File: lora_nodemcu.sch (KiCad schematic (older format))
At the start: 17 parts, among them U1 RFM95, U2 LM1117-3.3, U3 WeMos_mini

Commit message: fixed non connect on schematic and moved decoupling caps closer
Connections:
- net labels added: RF95_3V3, wemos_5V
- wire segments 65 -> 75
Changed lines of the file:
@@
 	4450 3500 4450 3950
 Wire Wire Line
-	3940 3400 4500 3400
+	3940 3400 3990 3400
 Wire Wire Line
 	5700 3500 5800 3500
@@
 	5800 3500 5800 3650
 Wire Wire Line
-	3910 3100 4500 3100
+	3910 3100 3990 3100
 Wire Wire Line
 	5900 3300 5700 3300
@@
 Wire Wire Line
 	5700 2800 5700 2700
-Wire Wire Line
-	7700 2150 7700 2500
 Wire Wire Line
 	7700 2500 7850 2500
@@
 	7000 3550 7000 3100
 Wire Wire Line
-	8100 4550 8600 4550
+	8100 4550 8350 4550
 Wire Wire Line
-	7050 4550 7500 4550
+	7050 4550 7300 4550
 Wire Wire Line
-	7800 4850 7800 5150
+	7800 4850 7800 5000
 Wire Wire Line
 	7300 4700 7300 4550
@@
 Connection ~ 8350 4550
 Wire Wire Line
-	7300 5000 8350 5000
+	7300 5000 7800 5000
 Wire Wire Line
 	8350 5000 8350 4900
 Connection ~ 7800 5000
 Wire Wire Line
-	8100 4475 8100 4650
+	8100 4475 8100 4550
 Connection ~ 8100 4550
 Wire Wire Line
@@
 	7160 2900 7850 2900
 Wire Wire Line
-	7380 2600 7380 2170
-Wire Wire Line
-	7700 1840 7700 1940
+	7380 2600 7380 2330
 Wire Wire Line
 	7700 2330 7630 2330
-Connection ~ 7700 2330
 Wire Wire Line
 	7430 2330 7380 2330
@@
 L device:C_Small C5
 U 1 1 5A1F028E
-P 9060 2310
-F 0 "C5" V 8831 2310 50  0000 C CNN
-F 1 "C_decoupling" V 8922 2310 50  0000 C CNN
-F 2 "Capacitors_SMD:C_0805_HandSoldering" H 9060 2310 50  0001 C CNN
-F 3 "" H 9060 2310 50  0001 C CNN
-	1    9060 2310
+P 9110 2310
+F 0 "C5" V 8881 2310 50  0000 C CNN
+F 1 "C_decoupling" V 8972 2310 50  0000 C CNN
+F 2 "Capacitors_SMD:C_0805_HandSoldering" H 9110 2310 50  0001 C CNN
+F 3 "" H 9110 2310 50  0001 C CNN
+	1    9110 2310
 	0    1    1    0
 $EndComp
 Wire Wire Line
-	8850 2500 8910 2500
+	8850 2500 8890 2500
 Wire Wire Line
-	8910 2500 8910 2310
+	8890 2500 8890 2310
 Wire Wire Line
-	8910 2310 8960 2310
+	8890 2310 9010 2310
 $Comp
 L power:GND #PWR010
@@
 $EndComp
 Wire Wire Line
-	9300 2310 9160 2310
+	9300 2310 9210 2310
 Wire Wire Line
 	4350 3950 4350 3400
 Connection ~ 4350 3400
+Wire Wire Line
+	7300 4550 7500 4550
+Wire Wire Line
+	8350 4550 8600 4550
+Wire Wire Line
+	7800 5000 7800 5150
+Wire Wire Line
+	7800 5000 8350 5000
+Wire Wire Line
+	8100 4550 8100 4650
+Wire Wire Line
+	7700 2330 7700 2500
+Wire Wire Line
+	7380 2330 7380 2170
+Wire Wire Line
+	3990 3400 4350 3400
+Wire Wire Line
+	3990 3100 4500 3100
+Wire Wire Line
+	4350 3400 4500 3400
+Wire Wire Line
+	7700 1840 7700 1940
+Connection ~ 7700 2330
+Wire Wire Line
+	7700 2140 7700 2330
+Text Label 7700 2350 0    50   ~ 0
+wemos_5V
+Text Label 4100 3100 0    50   ~ 0
+RF95_3V3
 $EndSCHEMATC

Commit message: changed antenna to solid gound pour
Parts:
- AE1: symbol device:Antenna_Shield -> lora_nodemcu-rescue:Antenna_Shield-device
- C1, C2: symbol device:C -> lora_nodemcu-rescue:C-device
- C3, C4, C5: symbol device:C_Small -> lora_nodemcu-rescue:C_Small-device
- L1, L2: symbol device:L_Core_Ferrite_Small -> lora_nodemcu-rescue:L_Core_Ferrite_Small-device
- R1, R2, R3, R4, R5, R6: symbol device:R -> lora_nodemcu-rescue:R-device
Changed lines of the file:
@@
 $EndComp
 $Comp
-L device:Antenna_Shield AE1
+L lora_nodemcu-rescue:Antenna_Shield-device AE1
 U 1 1 59CB0BD9
 P 4450 4150
@@
 $EndComp
 $Comp
-L device:R R3
+L lora_nodemcu-rescue:R-device R3
 U 1 1 59CC447A
 P 6350 3100
@@
 $EndComp
 $Comp
-L device:R R5
+L lora_nodemcu-rescue:R-device R5
 U 1 1 59CC4726
 P 6350 3650
@@
 $EndComp
 $Comp
-L device:R R6
+L lora_nodemcu-rescue:R-device R6
 U 1 1 59CC47A1
 P 6350 3800
@@
 $EndComp
 $Comp
-L device:R R4
+L lora_nodemcu-rescue:R-device R4
 U 1 1 59CF0F92
 P 6350 3450
@@
 $EndComp
 $Comp
-L device:R R2
+L lora_nodemcu-rescue:R-device R2
 U 1 1 59CF1001
 P 6350 2800
@@
 $EndComp
 $Comp
-L device:R R1
+L lora_nodemcu-rescue:R-device R1
 U 1 1 59CF1A56
 P 6350 2450
@@
 $EndComp
 $Comp
-L device:C C2
+L lora_nodemcu-rescue:C-device C2
 U 1 1 59DDA417
 P 8350 4750
@@
 $EndComp
 $Comp
-L device:C C1
+L lora_nodemcu-rescue:C-device C1
 U 1 1 59DDA458
 P 7300 4850
@@
 50Ohm
 $Comp
-L device:C_Small C4
+L lora_nodemcu-rescue:C_Small-device C4
 U 1 1 5A1CF19C
 P 7530 2330
@@
 $EndComp
 $Comp
-L device:L_Core_Ferrite_Small L2
+L lora_nodemcu-rescue:L_Core_Ferrite_Small-device L2
 U 1 1 5A1CF7A6
 P 7700 2040
@@
 $EndComp
 $Comp
-L device:C_Small C3
+L lora_nodemcu-rescue:C_Small-device C3
 U 1 1 5A1DF95C
 P 3990 3250
@@
 $EndComp
 $Comp
-L device:L_Core_Ferrite_Small L1
+L lora_nodemcu-rescue:L_Core_Ferrite_Small-device L1
 U 1 1 5A1DFA59
 P 3810 3100
@@
 Connection ~ 3990 3100
 $Comp
-L device:C_Small C5
+L lora_nodemcu-rescue:C_Small-device C5
 U 1 1 5A1F028E
 P 9110 2310

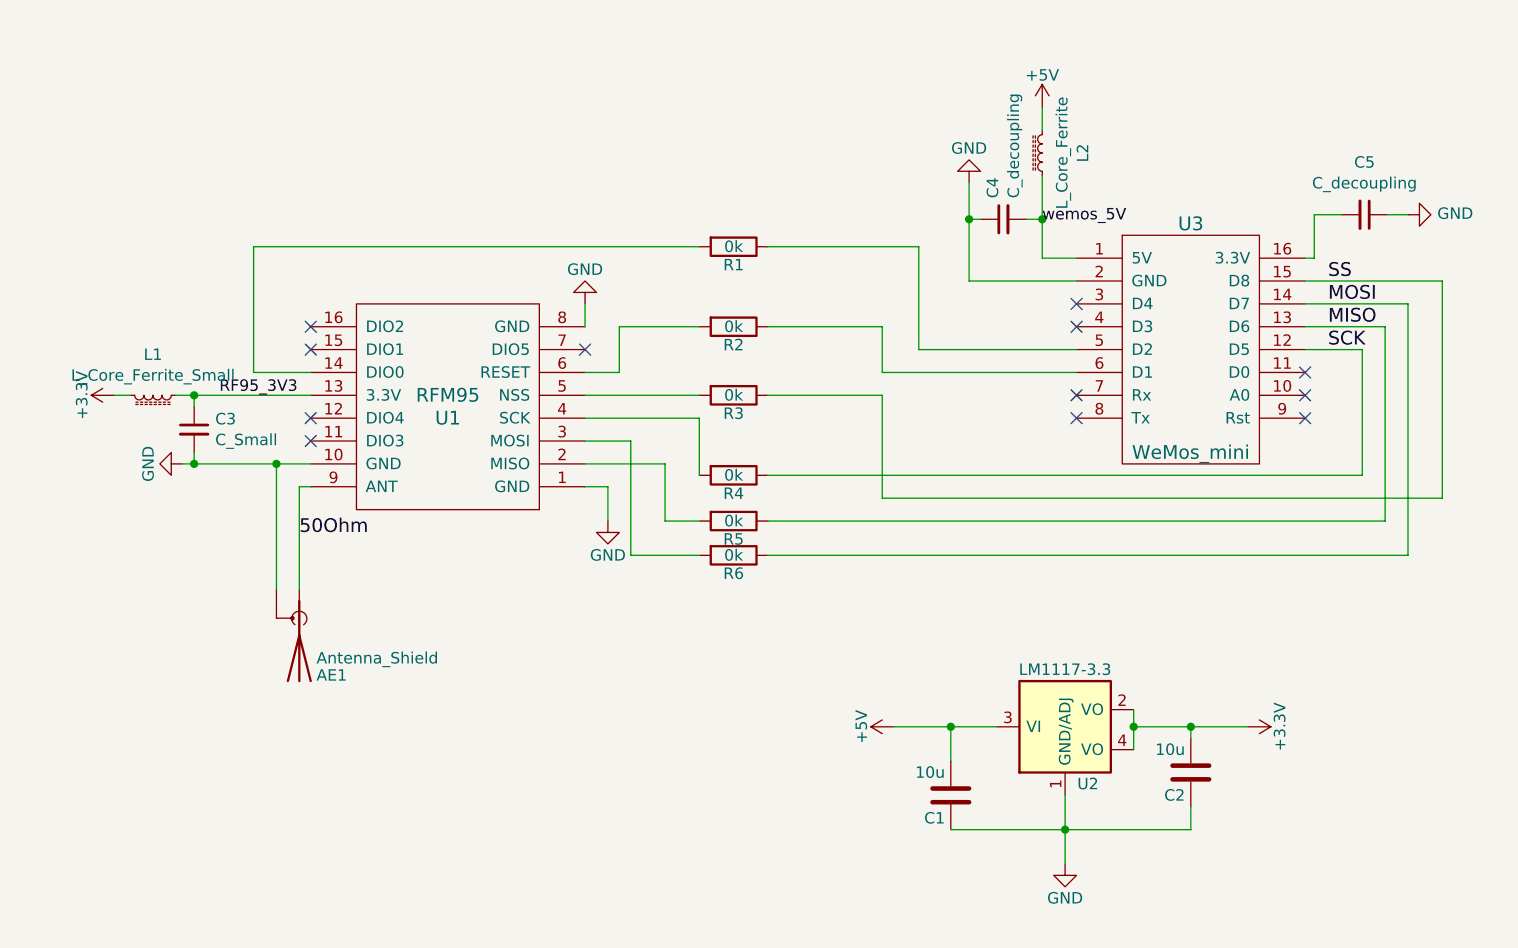
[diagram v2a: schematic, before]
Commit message: Changes erroneous 0k to JUMPERS
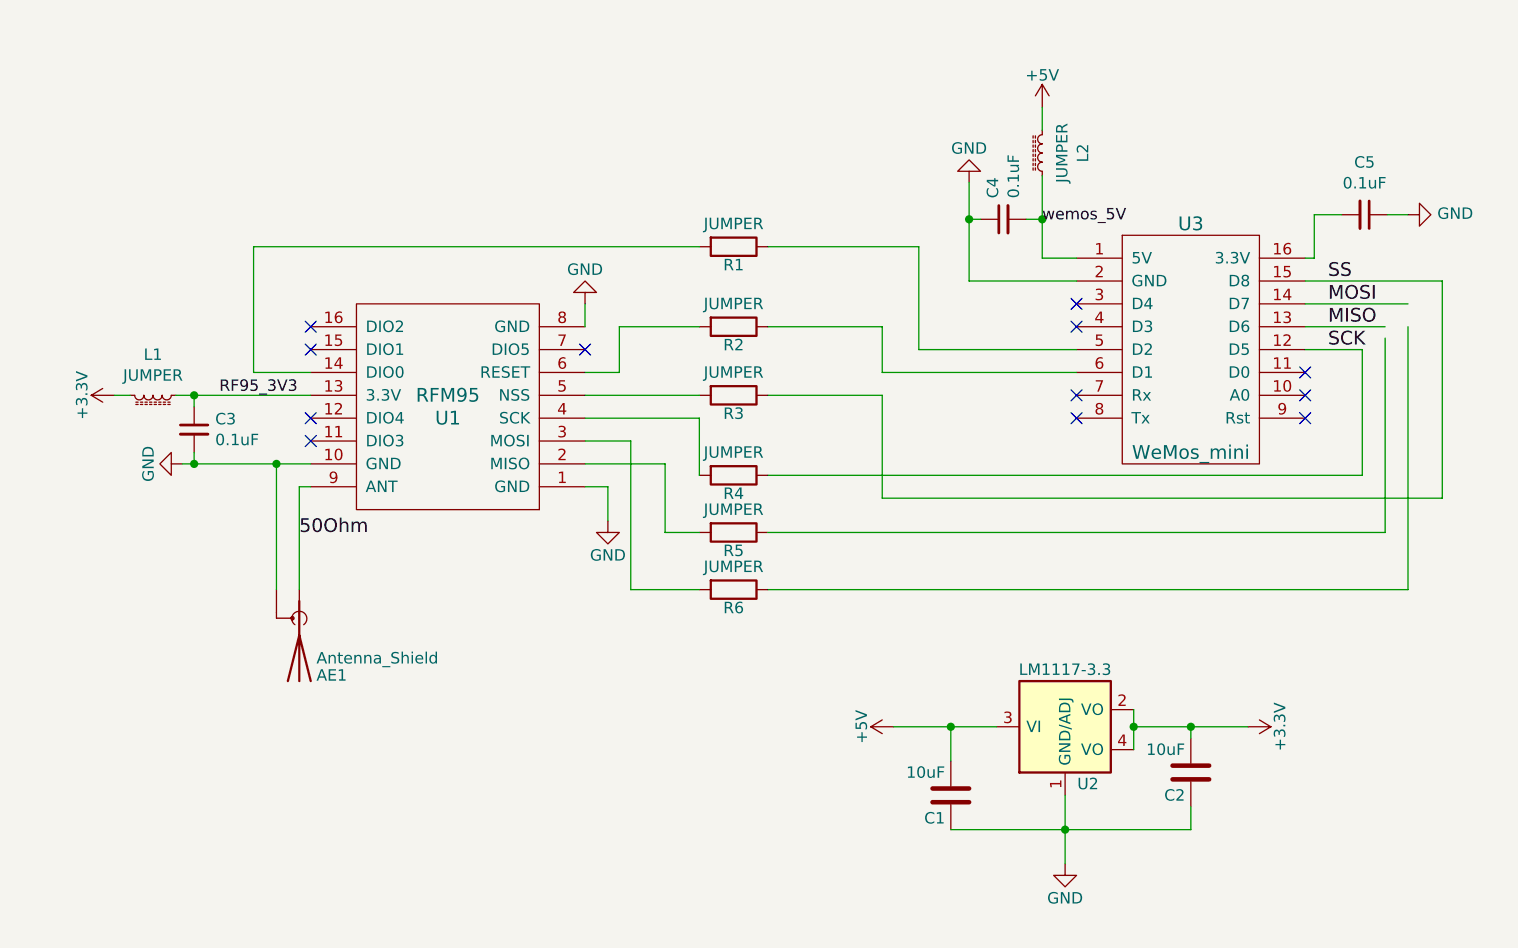
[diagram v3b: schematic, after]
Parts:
- C1, C2: value 10u -> 10uF
- C3: value C_Small -> 0.1uF
- C4, C5: value C_decoupling -> 0.1uF
- L1: value L_Core_Ferrite_Small -> JUMPER
- L2: value L_Core_Ferrite -> JUMPER
- R1, R2, R3, R4, R5, R6: value 0k -> JUMPER
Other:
- moved on the sheet: R5, R6
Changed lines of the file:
@@
 P 6350 3100
 F 0 "R3" V 6430 3100 50  0000 C CNN
-F 1 "0k" V 6350 3100 50  0000 C CNN
+F 1 "JUMPER" V 6250 3100 50  0000 C CNN
 F 2 "Resistors_SMD:R_0805_HandSoldering" V 6280 3100 50  0001 C CNN
 F 3 "" H 6350 3100 50  0001 C CNN
@@
 L lora_nodemcu-rescue:R-device R5
 U 1 1 59CC4726
-P 6350 3650
-F 0 "R5" V 6430 3650 50  0000 C CNN
-F 1 "0k" V 6350 3650 50  0000 C CNN
-F 2 "Resistors_SMD:R_0805_HandSoldering" V 6280 3650 50  0001 C CNN
-F 3 "" H 6350 3650 50  0001 C CNN
-	1    6350 3650
+P 6350 3700
+F 0 "R5" V 6430 3700 50  0000 C CNN
+F 1 "JUMPER" V 6250 3700 50  0000 C CNN
+F 2 "Resistors_SMD:R_0805_HandSoldering" V 6280 3700 50  0001 C CNN
+F 3 "" H 6350 3700 50  0001 C CNN
+	1    6350 3700
 	0    1    1    0
 $EndComp
@@
 L lora_nodemcu-rescue:R-device R6
 U 1 1 59CC47A1
-P 6350 3800
-F 0 "R6" V 6430 3800 50  0000 C CNN
-F 1 "0k" V 6350 3800 50  0000 C CNN
-F 2 "Resistors_SMD:R_0805_HandSoldering" V 6280 3800 50  0001 C CNN
-F 3 "" H 6350 3800 50  0001 C CNN
-	1    6350 3800
+P 6350 3950
+F 0 "R6" V 6430 3950 50  0000 C CNN
+F 1 "JUMPER" V 6250 3950 50  0000 C CNN
+F 2 "Resistors_SMD:R_0805_HandSoldering" V 6280 3950 50  0001 C CNN
+F 3 "" H 6350 3950 50  0001 C CNN
+	1    6350 3950
 	0    1    1    0
 $EndComp
@@
 P 6350 3450
 F 0 "R4" V 6430 3450 50  0000 C CNN
-F 1 "0k" V 6350 3450 50  0000 C CNN
+F 1 "JUMPER" V 6250 3450 50  0000 C CNN
 F 2 "Resistors_SMD:R_0805_HandSoldering" V 6280 3450 50  0001 C CNN
 F 3 "" H 6350 3450 50  0001 C CNN
@@
 P 6350 2800
 F 0 "R2" V 6430 2800 50  0000 C CNN
-F 1 "0k" V 6350 2800 50  0000 C CNN
+F 1 "JUMPER" V 6250 2800 50  0000 C CNN
 F 2 "Resistors_SMD:R_0805_HandSoldering" V 6280 2800 50  0001 C CNN
 F 3 "" H 6350 2800 50  0001 C CNN
@@
 P 6350 2450
 F 0 "R1" V 6430 2450 50  0000 C CNN
-F 1 "0k" V 6350 2450 50  0000 C CNN
+F 1 "JUMPER" V 6250 2450 50  0000 C CNN
 F 2 "Resistors_SMD:R_0805_HandSoldering" V 6280 2450 50  0001 C CNN
 F 3 "" H 6350 2450 50  0001 C CNN
@@
 P 8350 4750
 F 0 "C2" H 8375 4850 50  0000 L CNN
-F 1 "10u" H 8375 4650 50  0000 L CNN
+F 1 "10uF" H 8375 4650 50  0000 L CNN
 F 2 "Capacitors_SMD:C_0805_HandSoldering" H 8388 4600 50  0001 C CNN
 F 3 "" H 8350 4750 50  0001 C CNN
@@
 P 7300 4850
 F 0 "C1" H 7325 4950 50  0000 L CNN
-F 1 "10u" H 7325 4750 50  0000 L CNN
+F 1 "10uF" H 7325 4750 50  0000 L CNN
 F 2 "Capacitors_SMD:C_0805_HandSoldering" H 7338 4700 50  0001 C CNN
 F 3 "" H 7300 4850 50  0001 C CNN
@@
 P 7530 2330
 F 0 "C4" H 7622 2376 50  0000 L CNN
-F 1 "C_decoupling" H 7622 2285 50  0000 L CNN
+F 1 "0.1uF" H 7622 2285 50  0000 L CNN
 F 2 "Capacitors_SMD:C_0805_HandSoldering" H 7530 2330 50  0001 C CNN
 F 3 "" H 7530 2330 50  0001 C CNN
@@
 P 7700 2040
 F 0 "L2" V 7522 2040 50  0000 C CNN
-F 1 "L_Core_Ferrite" V 7613 2040 50  0000 C CNN
+F 1 "JUMPER" V 7613 2040 50  0000 C CNN
 F 2 "Inductors_SMD:L_0805_HandSoldering" H 7700 2040 50  0001 C CNN
 F 3 "" H 7700 2040 50  0001 C CNN
@@
 P 3990 3250
 F 0 "C3" H 4082 3296 50  0000 L CNN
-F 1 "C_Small" H 4082 3205 50  0000 L CNN
+F 1 "0.1uF" H 4082 3205 50  0000 L CNN
 F 2 "Capacitors_SMD:C_0805_HandSoldering" H 3990 3250 50  0001 C CNN
 F 3 "" H 3990 3250 50  0001 C CNN
@@
 P 3810 3100
 F 0 "L1" V 3632 3100 50  0000 C CNN
-F 1 "L_Core_Ferrite_Small" V 3723 3100 50  0000 C CNN
+F 1 "JUMPER" V 3723 3100 50  0000 C CNN
 F 2 "Inductors_SMD:L_0805_HandSoldering" H 3810 3100 50  0001 C CNN
 F 3 "" H 3810 3100 50  0001 C CNN
@@
 	4500 3000 4250 3000
 Wire Wire Line
-	6050 3400 6050 3650
+	6050 3400 6050 3700
 Wire Wire Line
 	5700 3200 6200 3200
@@
 	8850 2700 9300 2700
 Wire Wire Line
-	9300 3800 6500 3800
+	9300 3950 6500 3950
 Wire Wire Line
 	8850 2900 9100 2900
 Wire Wire Line
-	5900 3300 5900 3800
-Wire Wire Line
-	5900 3800 6200 3800
+	5900 3300 5900 3950
+Wire Wire Line
+	5900 3950 6200 3950
 Wire Wire Line
 	5850 2800 5850 3000
 Wire Wire Line
-	9300 2700 9300 3800
+	9300 2800 9300 3950
 Wire Wire Line
 	8850 2800 9200 2800
 Wire Wire Line
-	9200 2800 9200 3650
+	9200 2850 9200 3700
 Wire Wire Line
 	9100 2900 9100 3450
@@
 	9100 3450 6500 3450
 Wire Wire Line
-	9200 3650 6500 3650
-Wire Wire Line
-	6050 3650 6200 3650
+	9200 3700 6500 3700
+Wire Wire Line
+	6050 3700 6200 3700
 Wire Wire Line
 	9450 3550 9450 2600
@@
 P 9110 2310
 F 0 "C5" V 8881 2310 50  0000 C CNN
-F 1 "C_decoupling" V 8972 2310 50  0000 C CNN
+F 1 "0.1uF" V 8972 2310 50  0000 C CNN
 F 2 "Capacitors_SMD:C_0805_HandSoldering" H 9110 2310 50  0001 C CNN
 F 3 "" H 9110 2310 50  0001 C CNN

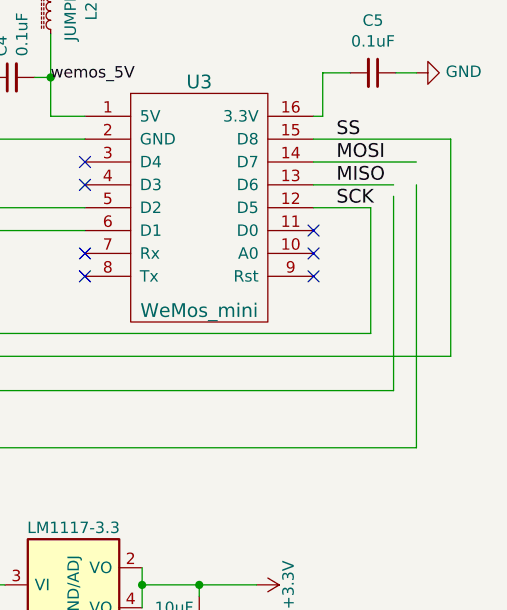
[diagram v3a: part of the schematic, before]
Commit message: connects two lines on schematic that I missed in last commit
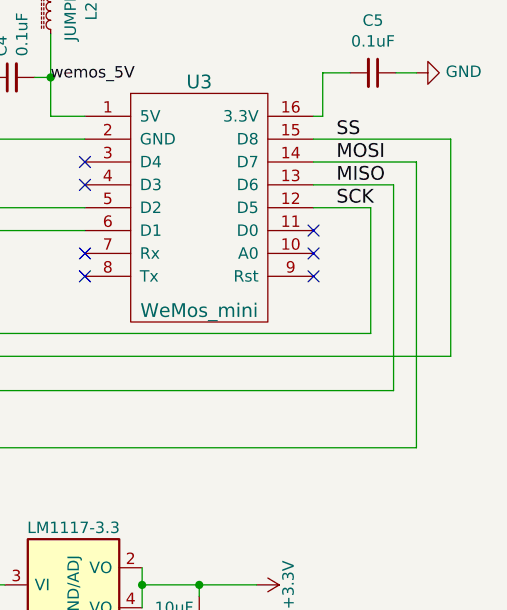
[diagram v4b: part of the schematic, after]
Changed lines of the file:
@@
 	5850 2800 5850 3000
 Wire Wire Line
-	9300 2800 9300 3950
-Wire Wire Line
 	8850 2800 9200 2800
-Wire Wire Line
-	9200 2850 9200 3700
 Wire Wire Line
 	9100 2900 9100 3450
@@
 Text Label 4100 3100 0    50   ~ 0
 RF95_3V3
+Wire Wire Line
+	9300 2700 9300 3950
+Wire Wire Line
+	9200 2800 9200 3700
 $EndSCHEMATC

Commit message: changes jumper resistors to bridged solder points
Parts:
- L1, L2: footprint Inductors_SMD:L_0805_HandSoldering -> Jumper:SolderJumper-2_P1.3mm_Bridged_Pad1.0x1.5mm
- R1, R2, R3, R4, R5, R6: footprint Resistors_SMD:R_0805_HandSoldering -> Jumper:SolderJumper-2_P1.3mm_Bridged_Pad1.0x1.5mm
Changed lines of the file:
@@
 F 0 "R3" V 6430 3100 50  0000 C CNN
 F 1 "JUMPER" V 6250 3100 50  0000 C CNN
-F 2 "Resistors_SMD:R_0805_HandSoldering" V 6280 3100 50  0001 C CNN
+F 2 "Jumper:SolderJumper-2_P1.3mm_Bridged_Pad1.0x1.5mm" V 6280 3100 50  0001 C CNN
 F 3 "" H 6350 3100 50  0001 C CNN
 	1    6350 3100
@@
 F 0 "R5" V 6430 3700 50  0000 C CNN
 F 1 "JUMPER" V 6250 3700 50  0000 C CNN
-F 2 "Resistors_SMD:R_0805_HandSoldering" V 6280 3700 50  0001 C CNN
+F 2 "Jumper:SolderJumper-2_P1.3mm_Bridged_Pad1.0x1.5mm" V 6280 3700 50  0001 C CNN
 F 3 "" H 6350 3700 50  0001 C CNN
 	1    6350 3700
@@
 F 0 "R6" V 6430 3950 50  0000 C CNN
 F 1 "JUMPER" V 6250 3950 50  0000 C CNN
-F 2 "Resistors_SMD:R_0805_HandSoldering" V 6280 3950 50  0001 C CNN
+F 2 "Jumper:SolderJumper-2_P1.3mm_Bridged_Pad1.0x1.5mm" V 6280 3950 50  0001 C CNN
 F 3 "" H 6350 3950 50  0001 C CNN
 	1    6350 3950
@@
 F 0 "R4" V 6430 3450 50  0000 C CNN
 F 1 "JUMPER" V 6250 3450 50  0000 C CNN
-F 2 "Resistors_SMD:R_0805_HandSoldering" V 6280 3450 50  0001 C CNN
+F 2 "Jumper:SolderJumper-2_P1.3mm_Bridged_Pad1.0x1.5mm" V 6280 3450 50  0001 C CNN
 F 3 "" H 6350 3450 50  0001 C CNN
 	1    6350 3450
@@
 F 0 "R2" V 6430 2800 50  0000 C CNN
 F 1 "JUMPER" V 6250 2800 50  0000 C CNN
-F 2 "Resistors_SMD:R_0805_HandSoldering" V 6280 2800 50  0001 C CNN
+F 2 "Jumper:SolderJumper-2_P1.3mm_Bridged_Pad1.0x1.5mm" V 6280 2800 50  0001 C CNN
 F 3 "" H 6350 2800 50  0001 C CNN
 	1    6350 2800
@@
 F 0 "R1" V 6430 2450 50  0000 C CNN
 F 1 "JUMPER" V 6250 2450 50  0000 C CNN
-F 2 "Resistors_SMD:R_0805_HandSoldering" V 6280 2450 50  0001 C CNN
+F 2 "Jumper:SolderJumper-2_P1.3mm_Bridged_Pad1.0x1.5mm" V 6280 2450 50  0001 C CNN
 F 3 "" H 6350 2450 50  0001 C CNN
 	1    6350 2450
@@
 F 0 "L2" V 7522 2040 50  0000 C CNN
 F 1 "JUMPER" V 7613 2040 50  0000 C CNN
-F 2 "Inductors_SMD:L_0805_HandSoldering" H 7700 2040 50  0001 C CNN
+F 2 "Jumper:SolderJumper-2_P1.3mm_Bridged_Pad1.0x1.5mm" H 7700 2040 50  0001 C CNN
 F 3 "" H 7700 2040 50  0001 C CNN
 	1    7700 2040
@@
 F 0 "L1" V 3632 3100 50  0000 C CNN
 F 1 "JUMPER" V 3723 3100 50  0000 C CNN
-F 2 "Inductors_SMD:L_0805_HandSoldering" H 3810 3100 50  0001 C CNN
+F 2 "Jumper:SolderJumper-2_P1.3mm_Bridged_Pad1.0x1.5mm" H 3810 3100 50  0001 C CNN
 F 3 "" H 3810 3100 50  0001 C CNN
 	1    3810 3100
